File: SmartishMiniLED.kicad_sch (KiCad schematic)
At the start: 28 parts, among them J1 USB_C_Receptacle_USB2.0, J2 BUTTON, J3 Screw_Terminal_01x03, P1 NeopixelStripPads, Q1 MMBT2222, Q2 MMBT2222, SW1 TL3342, SW2 TL3342, U1 ESP32-PICO-D4, U2 AP2112K-3.3, U3 CH340C, U4 SN74LVC2T45DCUR, U5 TSOP382xx

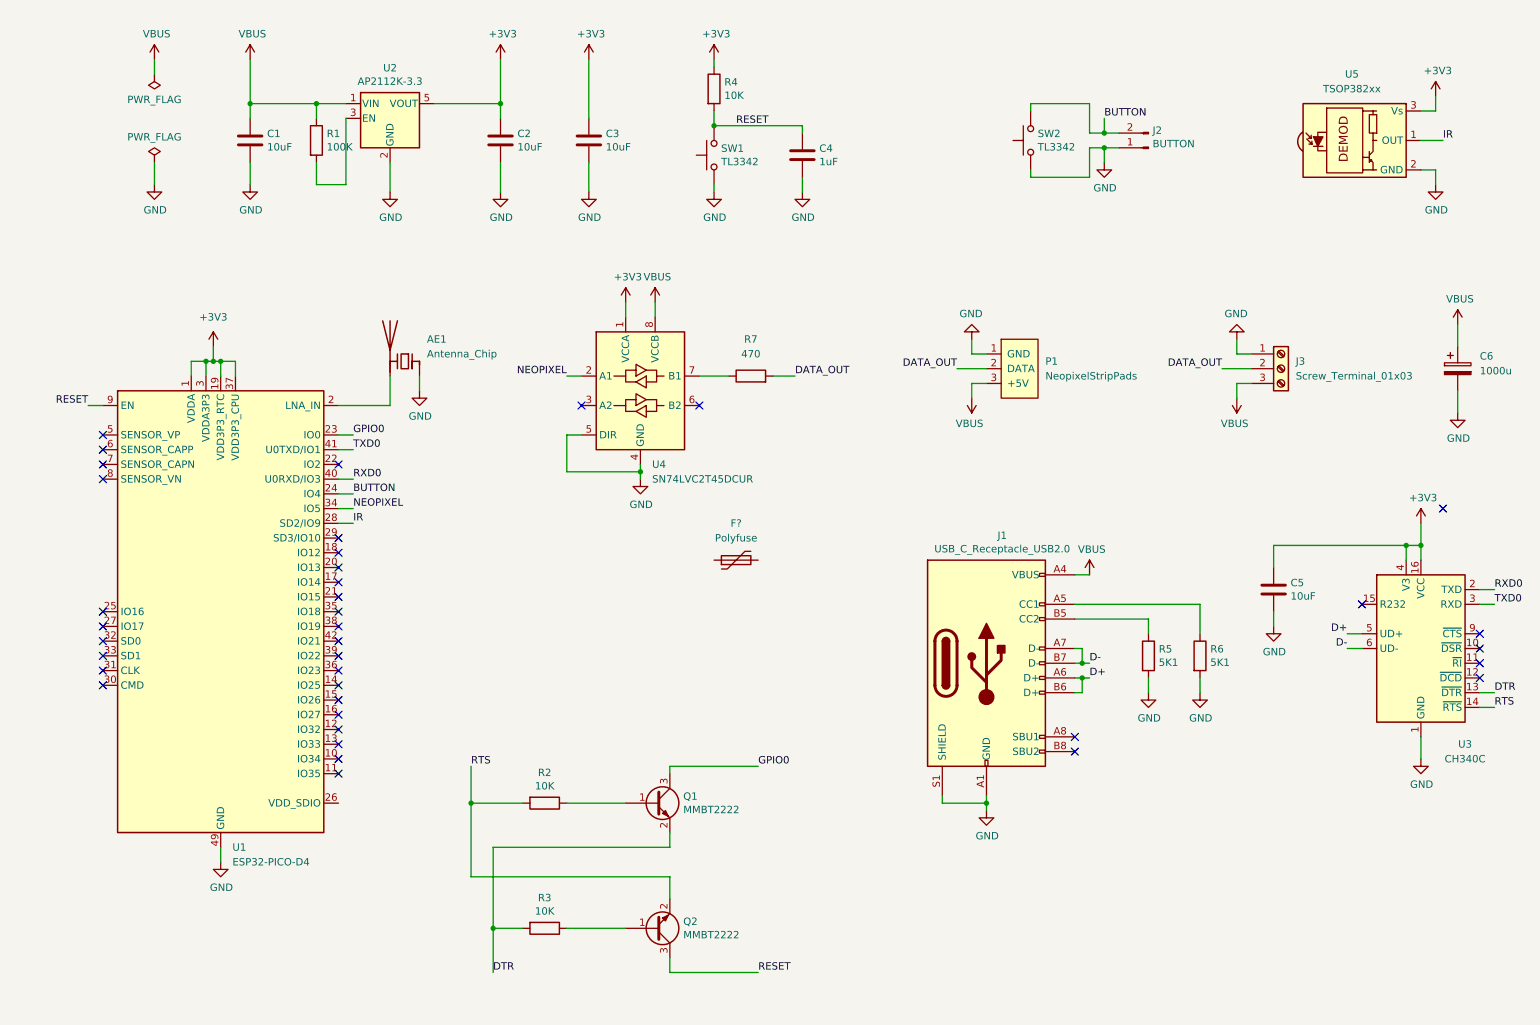
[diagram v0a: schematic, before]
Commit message: Added MOSFET to switch LED power and fixed ERC errors
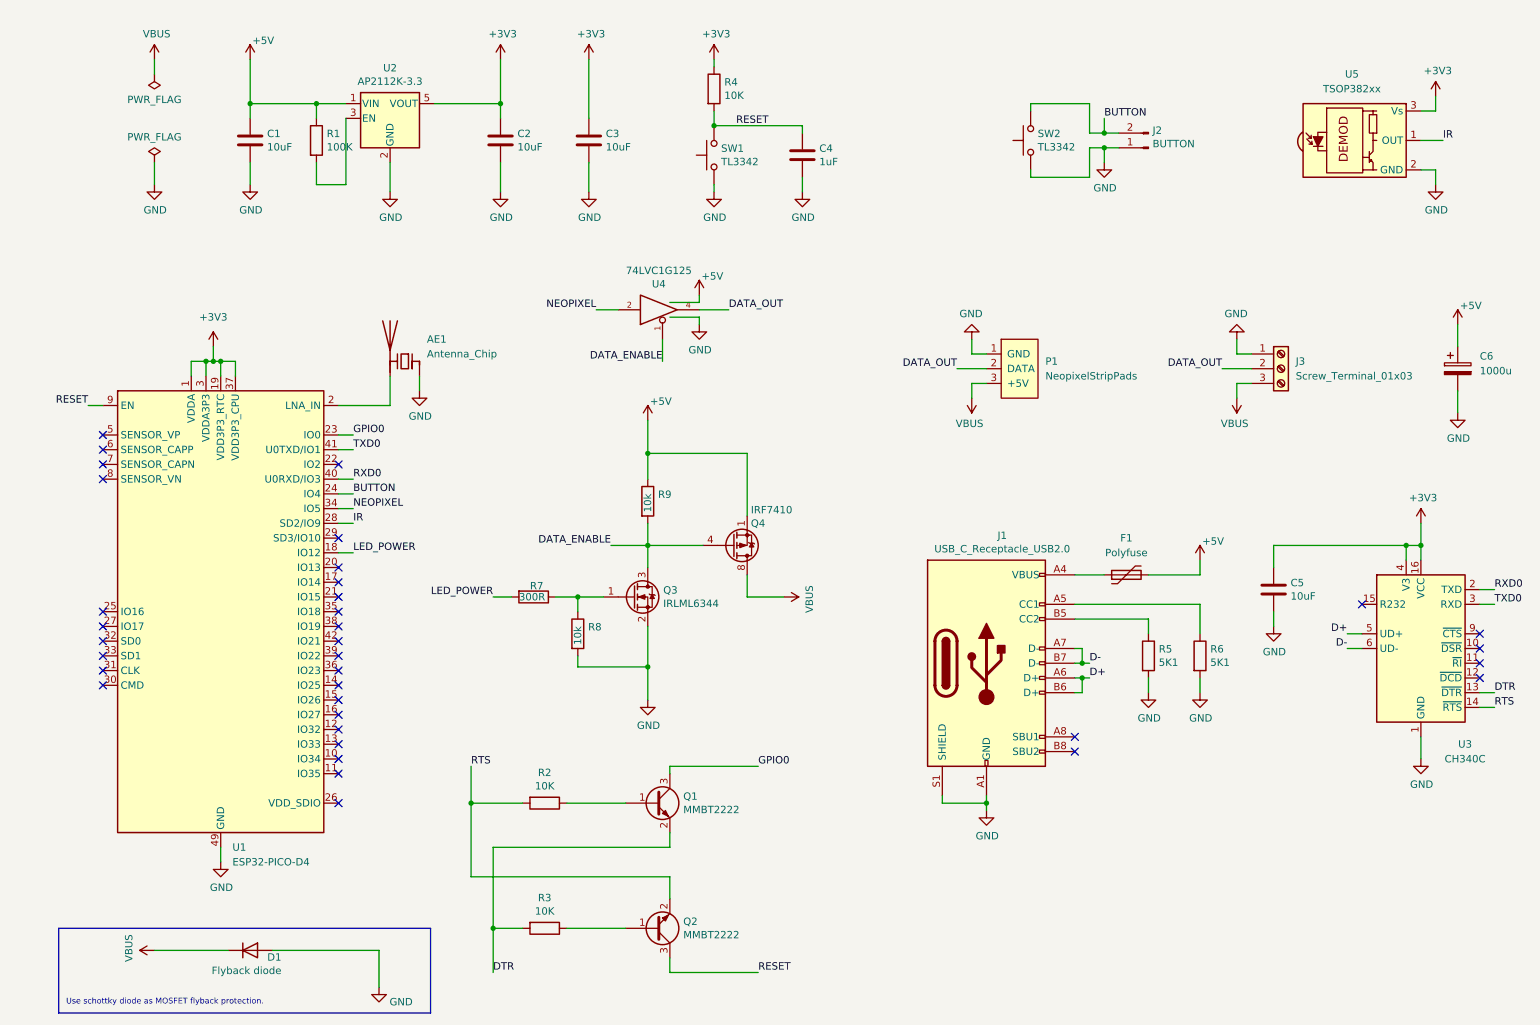
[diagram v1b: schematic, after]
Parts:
- removed U4: SN74LVC2T45DCUR, Package_SO:VSSOP-8_2.4x2.1mm_P0.5mm, symbol Logic_LevelTranslator:SN74LVC2T45DCUR
- added D1: Flyback diode, Diode_SMD:D_SMA_Handsoldering, symbol Device:D
- added Q3: IRLML6344, Package_TO_SOT_SMD:SOT-23, symbol Transistor_FET:TSM2302CX
- added Q4: IRF7410, Package_SO:SOIC-8_3.9x4.9mm_P1.27mm, symbol Transistor_FET:IRF7404
- added R8, R9: 10k, Resistor_SMD:R_0805_2012Metric_Pad1.20x1.40mm_HandSolder, symbol Device:R
- added U4: 74LVC1G125, Package_TO_SOT_SMD:SOT-23-5, symbol 74xGxx:74LVC1G125
- R7: value 470 -> 300R; footprint Package_DIP:DIP-14_W7.62mm_SMDSocket_SmallPads -> Resistor_SMD:R_0805_2012Metric_Pad1.20x1.40mm_HandSolder; LCSC (none) -> C17617
- gave numbers to parts that had none: 1
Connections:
- net GND is gone; now on net +5V: AE1.1 (FEED), C1.2, C2.2, C3.2, C4.1, C5.2, C6.2, J1.A1 (GND), J1.A12 (GND), J1.B1 (GND), J1.B12 (GND), J1.S1 (SHIELD), J2.1 (Pin_1), J3.1 (Pin_1), P1.1 (GND), R5.2, R6.2, SW1.1, SW2.1, U1.49 (GND), U2.2 (GND), U3.1 (GND), U5.2 (GND)
- net DATA_OUT: now also U4.4; no longer R7.2
- net NEOPIXEL: now also U4.2
- net VBUS: now also D1.1 (K), Q4.5 (D), Q4.6 (D), Q4.7 (D), Q4.8 (D); no longer C1.1, C6.1, J1.A4 (VBUS), J1.A9 (VBUS), J1.B4 (VBUS), J1.B9 (VBUS), R1.1, U2.1 (VIN)
- net at R7.1: now also Q3.1 (G), R8.1
- net at F1.1: now also J1.A4 (VBUS), J1.A9 (VBUS), J1.B4 (VBUS), J1.B9 (VBUS)
- net +5V: now reaches F1.2
- net +5V: now also C1.1, C6.1, R1.1, U2.1 (VIN), D1.2 (A), Q3.2 (S), Q4.1 (S), Q4.2 (S), Q4.3 (S), R8.2, R9.1, U4.3 (GND), U4.5 (VCC)
- net LED_POWER: now reaches U1.18 (IO12)
- net LED_POWER: now also R7.2
- new net DATA_ENABLE: Q3.3 (D), Q4.4 (G), R9.2, U4.1
- no-connect marks 38 -> 35
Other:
- note added: "Use schottky diode as MOSFET flyback protection."
- moved on the sheet: F1

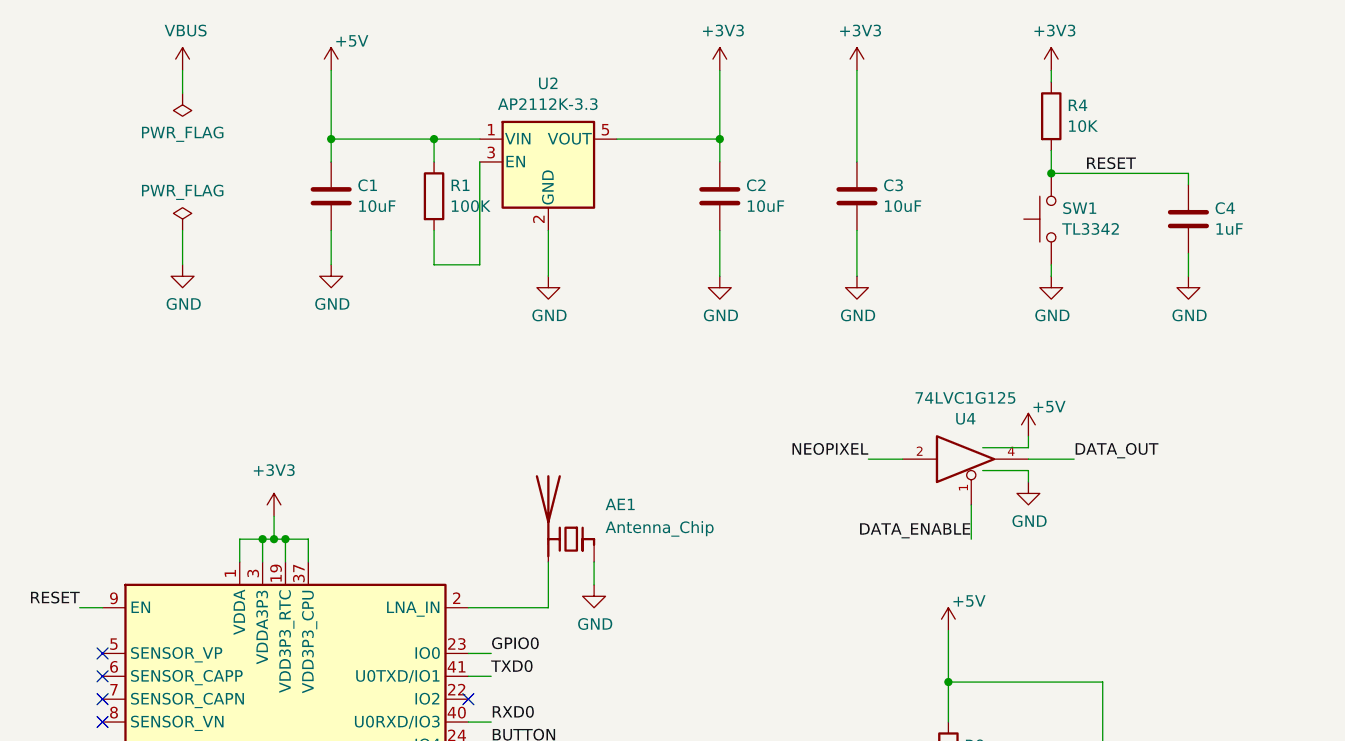
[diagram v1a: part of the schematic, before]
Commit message: WIP Fixed a few bugs in schematic and made a start on the PCB layout
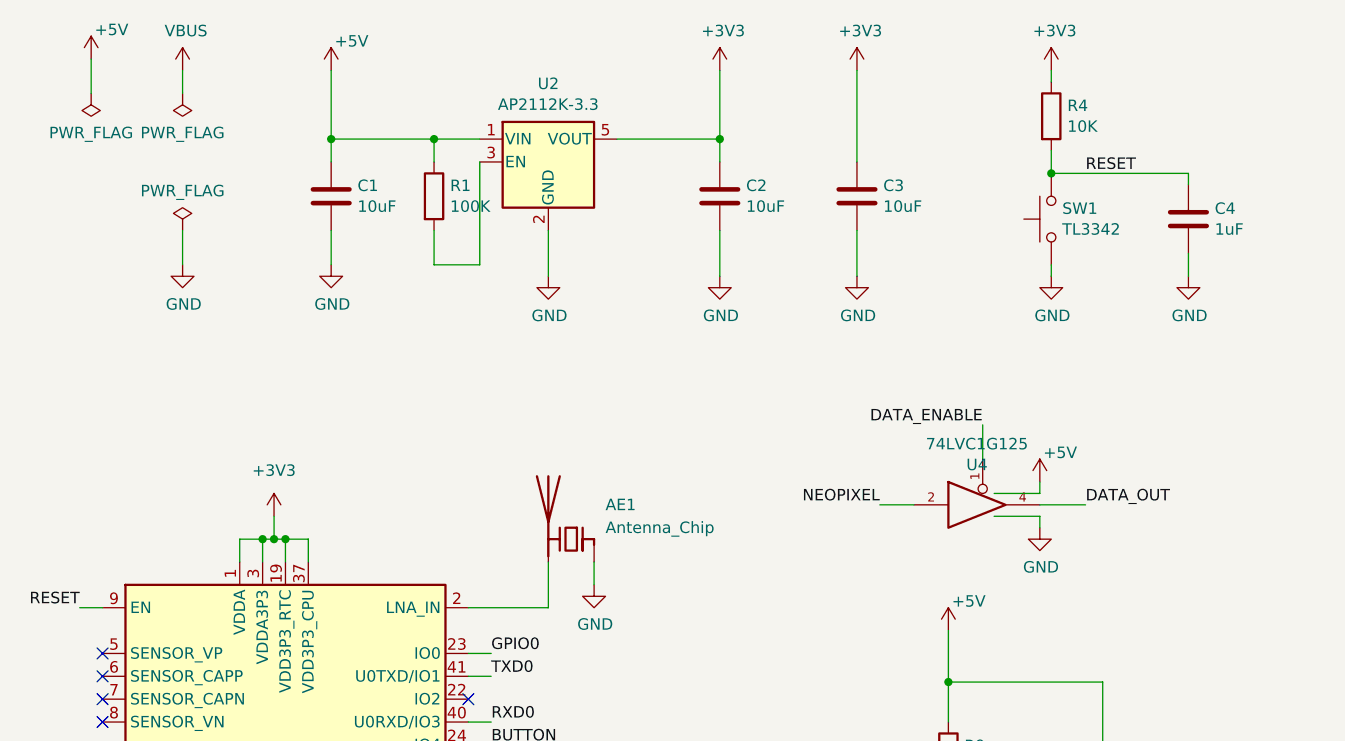
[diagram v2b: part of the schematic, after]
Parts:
- AE1: footprint (none) -> RF_Antenna:Texas_SWRA117D_2.4GHz_Left
- C6: footprint (none) -> Capacitor_SMD:CP_Elec_10x10
- F1: footprint (none) -> Fuse:Fuse_1206_3216Metric
- J3: footprint (none) -> TerminalBlock_Phoenix:TerminalBlock_Phoenix_MPT-0,5-3-2.54_1x03_P2.54mm_Horizontal
- P1: footprint (none) -> SmartishMiniLED:LedStripPads
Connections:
- net +5V: no longer AE1.1 (FEED), C1.2, C2.2, C3.2, C4.1, C5.2, C6.2, D1.2 (A), J1.A1 (GND), J1.A12 (GND), J1.B1 (GND), J1.B12 (GND), J1.S1 (SHIELD), J2.1 (Pin_1), J3.1 (Pin_1), P1.1 (GND), Q3.2 (S), R5.2, R6.2, R8.2, SW1.1, SW2.1, U1.49 (GND), U2.2 (GND), U3.1 (GND), U4.3 (GND), U5.2 (GND)
- new net GND: AE1.1 (FEED), C1.2, C2.2, C3.2, C4.1, C5.2, C6.2, D1.2 (A), J1.A1 (GND), J1.A12 (GND), J1.B1 (GND), J1.B12 (GND), J1.S1 (SHIELD), J2.1 (Pin_1), J3.1 (Pin_1), P1.1 (GND), Q3.2 (S), R5.2, R6.2, R8.2, SW1.1, SW2.1, U1.49 (GND), U2.2 (GND), U3.1 (GND), U4.3 (GND), U5.2 (GND)
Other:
- moved on the sheet: U4

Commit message: Initial layout
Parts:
- removed C4: 1uF, Capacitor_SMD:C_0805_2012Metric, symbol Device:C
- removed R4: 10K, Resistor_SMD:R_0805_2012Metric, symbol Device:R
- removed SW1: TL3342, Button_Switch_SMD:SW_SPST_TL3342, symbol Switch:SW_Push
- added P2: NeopixelStripPads, SmartishMiniLED:LedStripPads, symbol neopixelstrippads:NeopixelStripPads
- AE1: footprint RF_Antenna:Texas_SWRA117D_2.4GHz_Left -> RF_Antenna:Texas_SWRA117D_2.4GHz_Right
- J3: footprint TerminalBlock_Phoenix:TerminalBlock_Phoenix_MPT-0,5-3-2.54_1x03_P2.54mm_Horizontal -> TerminalBlock_TE-Connectivity:TerminalBlock_TE_282834-3_1x03_P2.54mm_Horizontal
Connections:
- net +5V: no longer C6.1
- net DATA_OUT: now also P2.2 (DATA)
- net GND: now also P2.1 (GND)
- net VBUS: now also C6.1, P2.3 (+5V)
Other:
- moved on the sheet: J2, P1, SW2, U4, U5

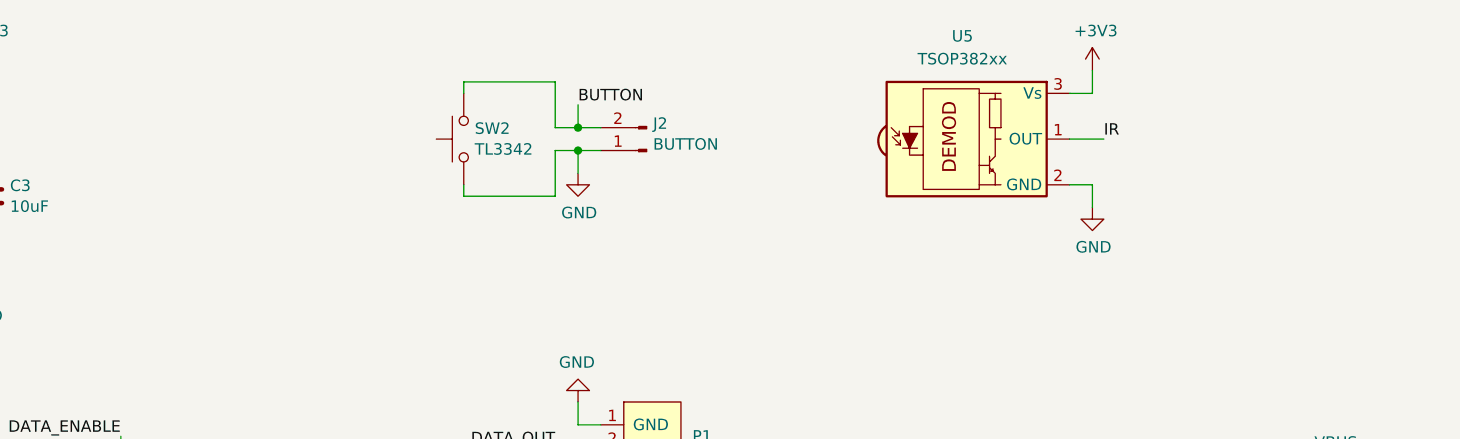
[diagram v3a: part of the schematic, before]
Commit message: DRC check fixes
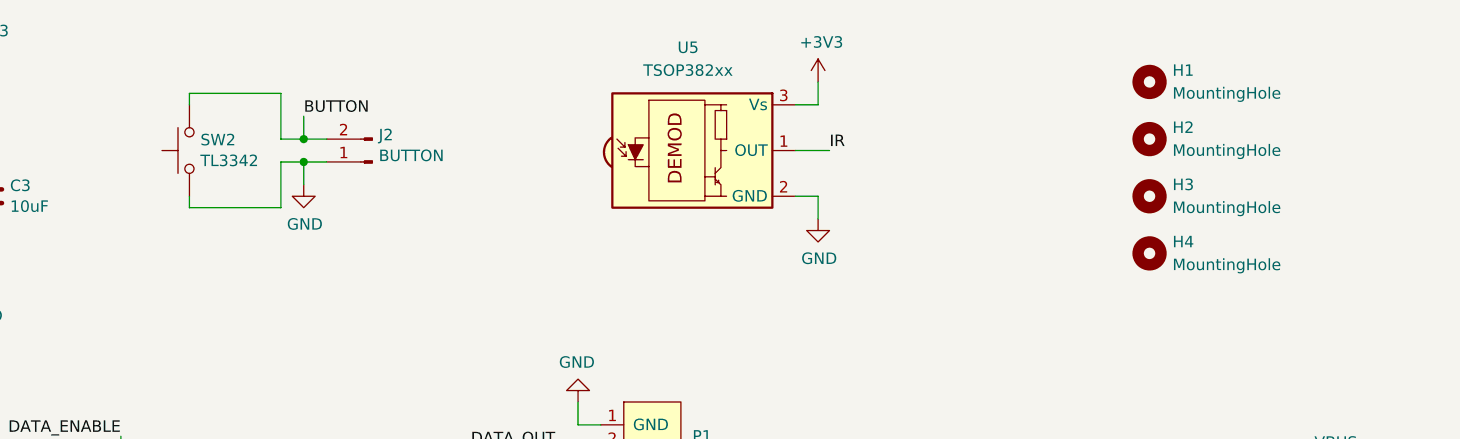
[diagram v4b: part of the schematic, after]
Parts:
- added H1, H2, H3, H4: MountingHole, MountingHole:MountingHole_3.2mm_M3, symbol Mechanical:MountingHole
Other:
- moved on the sheet: J2, SW2, U5

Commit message: 2nd attempt to fix DRC errors
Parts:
- AE1: footprint RF_Antenna:Texas_SWRA117D_2.4GHz_Right -> SmartishMiniLED:Texas_SWRA117D_2.4GHz_Right
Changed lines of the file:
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@@
       (effects (font (size 1.27 1.27)) (justify right))
     )
-    (property "Footprint" "RF_Antenna:Texas_SWRA117D_2.4GHz_Right" (id 2) (at 85.09 74.295 0)
+    (property "Footprint" "SmartishMiniLED:Texas_SWRA117D_2.4GHz_Right" (id 2) (at 85.09 74.295 0)
       (effects (font (size 1.27 1.27)) hide)
     )
@@
     )
     (path "/76b827cb-1c34-444d-8423-f6c16b1077b9"
-      (reference "AE1") (unit 1) (value "Antenna_Chip") (footprint "RF_Antenna:Texas_SWRA117D_2.4GHz_Right")
+      (reference "AE1") (unit 1) (value "Antenna_Chip") (footprint "SmartishMiniLED:Texas_SWRA117D_2.4GHz_Right")
     )
     (path "/00000000-0000-0000-0000-00005f9ef301"
